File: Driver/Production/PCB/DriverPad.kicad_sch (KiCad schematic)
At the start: 18 parts, among them SW1 SW_Push, SW2 SW_Push, SW3 SW_Push, SW4 SW_Push, SW5 SW_Push, SW6 SW_Push, SW7 SW_Push, SW8 SW_Push, U1 MOUDLE-SEEEDUINO-XIAO, U2 ER_OLEDM0.91_1x-I2C

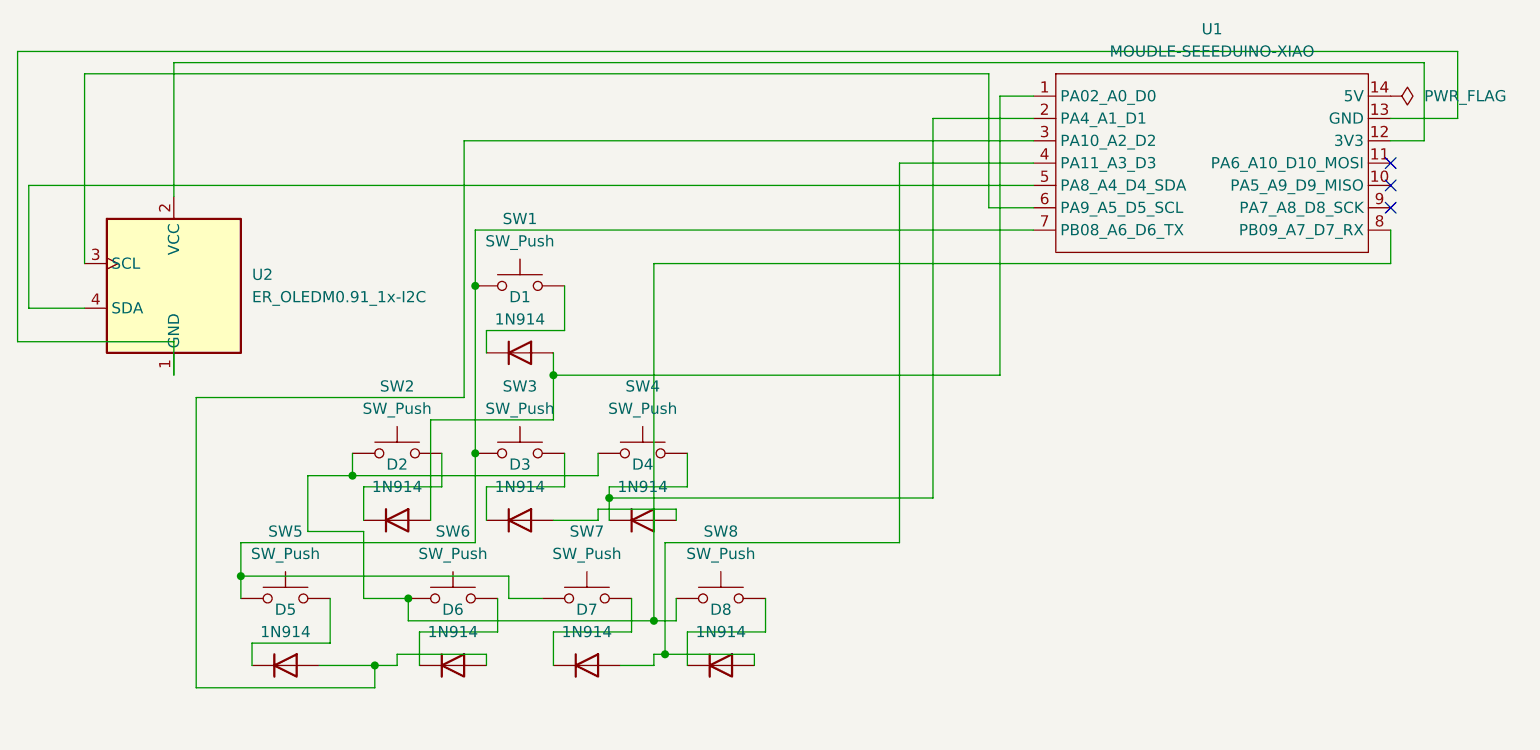
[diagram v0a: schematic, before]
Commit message: Fixed matrix wiring issues
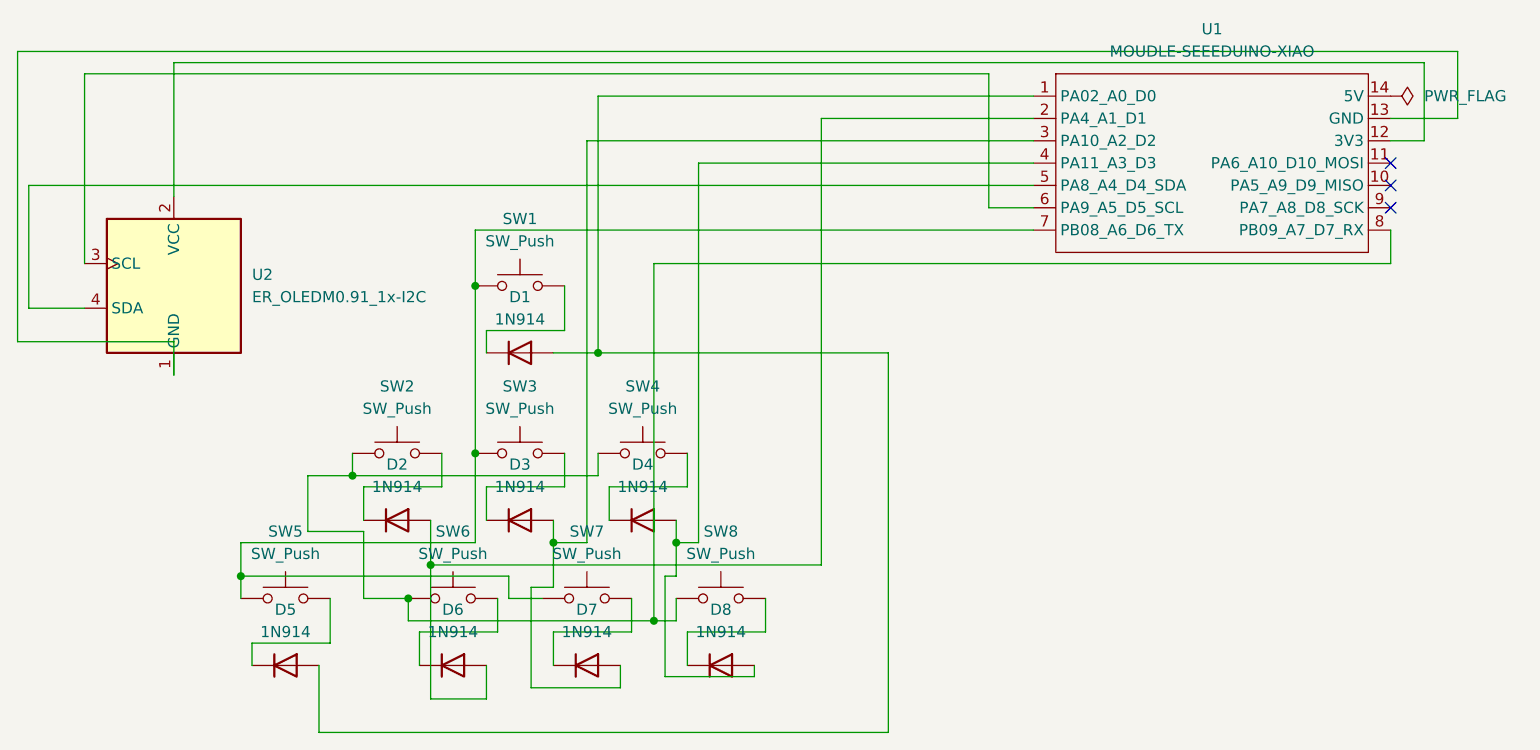
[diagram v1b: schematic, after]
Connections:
- net at D1.2 (A), U1.1 (PA02_A0_D0): now also D5.2 (A); no longer D2.2 (A)
- net at D4.1 (K), SW4.2: no longer U1.2 (PA4_A1_D1)
- net at D4.2 (A): now also D8.2 (A), U1.4 (PA11_A3_D3); no longer D3.2 (A)
- new net: D2.2 (A), D6.2 (A), U1.2 (PA4_A1_D1)
- new net: D3.2 (A), D7.2 (A), U1.3 (PA10_A2_D2)
